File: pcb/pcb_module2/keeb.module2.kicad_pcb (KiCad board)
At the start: 2 copper layers, 1 part, among them U2 0.91

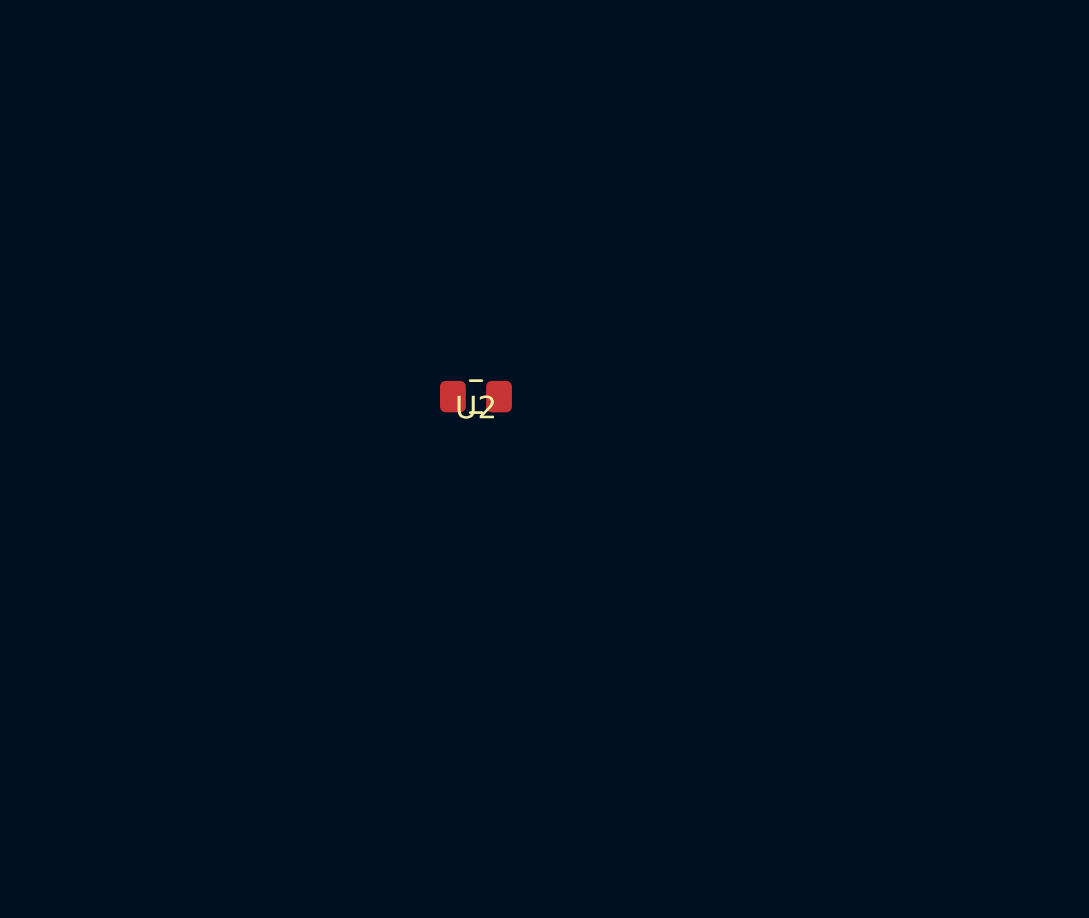
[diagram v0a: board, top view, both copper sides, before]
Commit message: Rev 1 of module 2 & updated all-in-one cad drawing
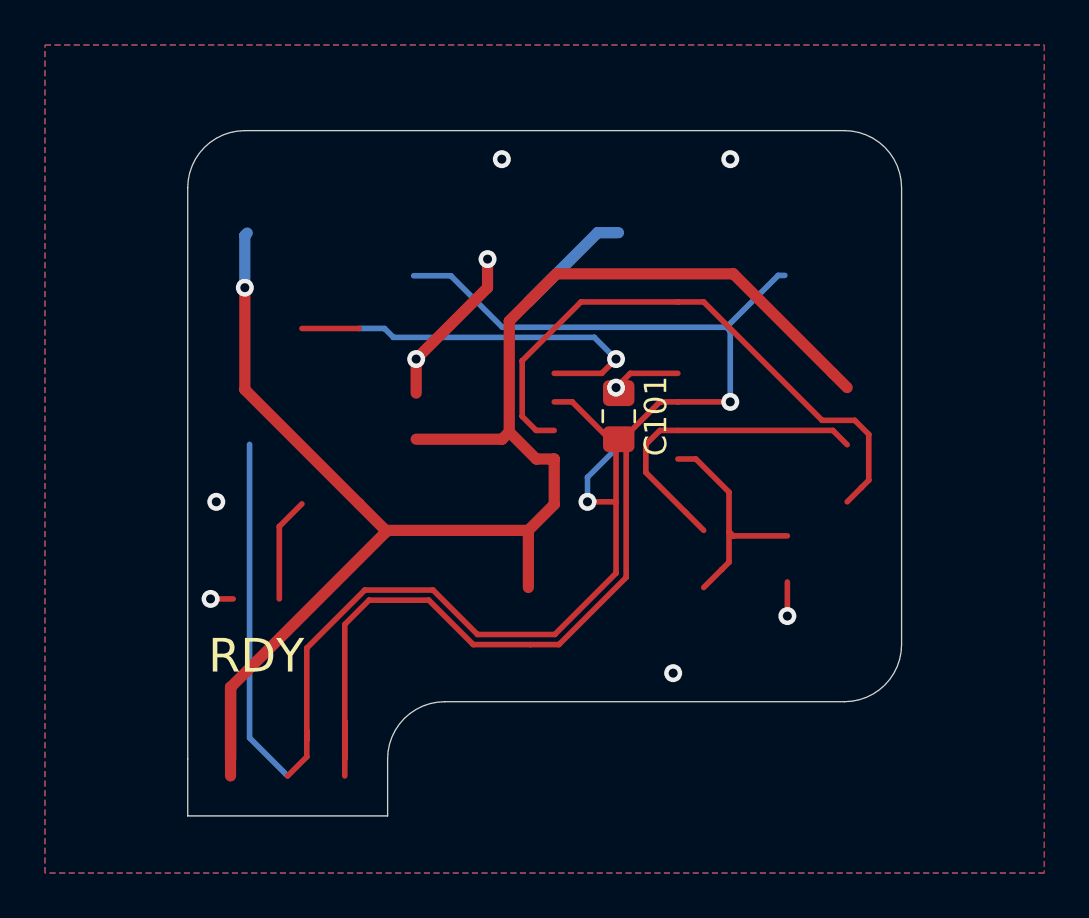
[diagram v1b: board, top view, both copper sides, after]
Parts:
- moved U2 6.41 mm to (94.1, 45.7), turned to 270 degrees
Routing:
- net VCC: track 0.00 -> 80.3 mm, vias 0 -> 1
- net /SCL_IN: track 0.00 -> 56.8 mm, vias 0 -> 1
- net /SDA_IN: track 0.00 -> 52.3 mm, vias 0 -> 1
- net /SDA: track 0.00 -> 26.5 mm
- net Net-(R104-Pad2): track 0.00 -> 17.5 mm, vias 0 -> 1
- net /SCK: track 0.00 -> 14.4 mm
- net GND: track 0.00 -> 12.8 mm, vias 0 -> 9
- net Net-(C102-Pad1): track 0.00 -> 10.3 mm
- net Net-(D101-Pad2): track 0.00 -> 4.65 mm
- added copper zone on B.Cu, net GND
- added copper zone on F.Cu, net GND
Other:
- board outline added: 31.8 x 30.5 mm
- board text added: "RDY"
